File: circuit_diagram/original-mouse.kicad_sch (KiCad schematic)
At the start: 106 parts, among them J1 Conn_02x03_Odd_Even, J2 Conn_02x03_Odd_Even, J3 Conn_01x08, Q1 TJ8S06M3L, Q10 ST-1KL3A, Q2 BSS138, Q3 BSS138, Q4 BSS138, Q5 BSS138, Q6 BSS138, Q7 ST-1KL3A, Q8 ST-1KL3A, Q9 ST-1KL3A, SW1 SW_SPDT, SW2 TS-06104, SW3 TS-06104, SW4 TS-06104, SW5 SW_Push, SW6 SW_Push, U1 NJM7805SDL1, U2 NJM2845DL1-33, U3 PKMCS0909E4000-R1, U4 ICM-20649, U5 DRV8835, U6 STM32F405RGTx

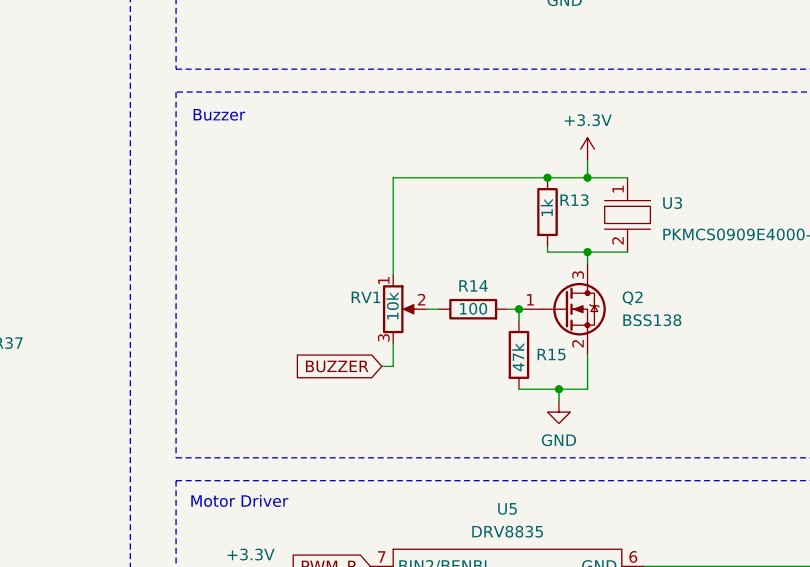
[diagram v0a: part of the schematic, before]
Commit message: ブザー回路を修正
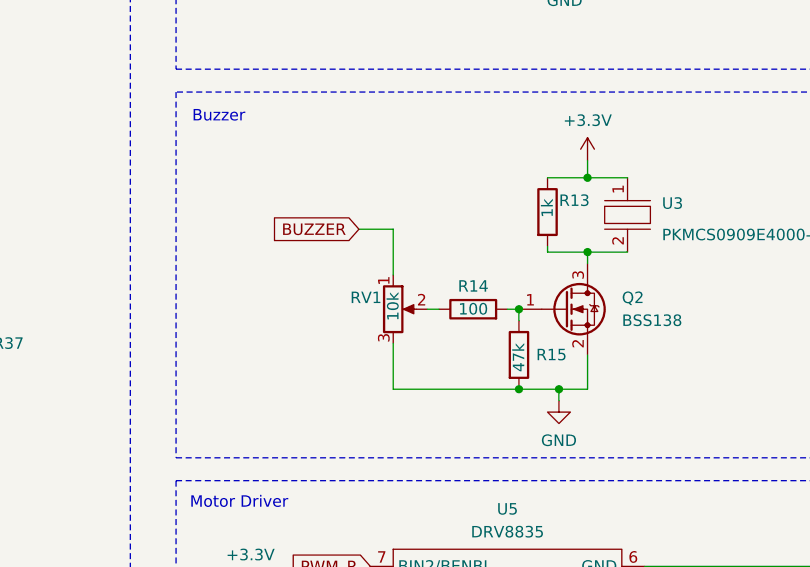
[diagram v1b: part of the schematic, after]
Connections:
- net +3.3V: no longer RV1.1
- net BUZZER: now also RV1.1; no longer RV1.3
- net GND: now also RV1.3
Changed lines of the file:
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@@
   (junction (at 271.78 129.54) (diameter 0) (color 0 0 0 0)
   )
-  (junction (at 353.695 169.545) (diameter 0) (color 0 0 0 0)
-  )
   (junction (at 118.11 264.16) (diameter 0) (color 0 0 0 0)
   )
@@
   )
   (junction (at 237.49 101.6) (diameter 0) (color 0 0 0 0)
+  )
+  (junction (at 350.52 193.04) (diameter 0) (color 0 0 0 0)
   )
   (junction (at 248.92 226.06) (diameter 0) (color 0 0 0 0)
@@
     (stroke (width 0) (type default))
   )
-  (wire (pts (xy 336.55 190.5) (xy 335.28 190.5))
-    (stroke (width 0) (type default))
-  )
   (wire (pts (xy 124.46 194.31) (xy 152.4 194.31))
     (stroke (width 0) (type default))
@@
     (stroke (width 0) (type default))
   )
-  (wire (pts (xy 336.55 169.545) (xy 336.55 180.34))
-    (stroke (width 0) (type default))
-  )
   (wire (pts (xy 89.535 219.075) (xy 89.535 220.98))
     (stroke (width 0) (type default))
@@
     (stroke (width 0) (type default))
   )
+  (wire (pts (xy 336.55 175.26) (xy 332.74 175.26))
+    (stroke (width 0) (type default))
+  )
   (wire (pts (xy 251.46 68.58) (xy 251.46 71.12))
     (stroke (width 0) (type default))
@@
     (stroke (width 0) (type default))
   )
-  (wire (pts (xy 353.695 169.545) (xy 336.55 169.545))
-    (stroke (width 0) (type default))
-  )
   (wire (pts (xy 246.38 119.38) (xy 246.38 127))
     (stroke (width 0) (type default))
@@
     (stroke (width 0) (type default))
   )
+  (wire (pts (xy 336.55 180.34) (xy 336.55 175.26))
+    (stroke (width 0) (type default))
+  )
   (wire (pts (xy 43.18 48.26) (xy 53.34 48.26))
     (stroke (width 0) (type default))
@@
     (stroke (width 0) (type default))
   )
+  (wire (pts (xy 336.55 193.04) (xy 350.52 193.04))
+    (stroke (width 0) (type default))
+  )
   (wire (pts (xy 243.84 116.84) (xy 248.92 116.84))
     (stroke (width 0) (type default))
@@
     (stroke (width 0) (type default))
   )
+  (wire (pts (xy 336.55 187.96) (xy 336.55 193.04))
+    (stroke (width 0) (type default))
+  )
   (wire (pts (xy 108.585 215.9) (xy 108.585 219.075))
     (stroke (width 0) (type default))
@@
   )
   (wire (pts (xy 386.08 223.52) (xy 386.08 225.425))
-    (stroke (width 0) (type default))
-  )
-  (wire (pts (xy 336.55 187.96) (xy 336.55 190.5))
     (stroke (width 0) (type default))
   )
@@
     )
   )
-  (global_label "BUZZER" (shape input) (at 335.28 190.5 180) (fields_autoplaced)
+  (global_label "BUZZER" (shape input) (at 332.74 175.26 180) (fields_autoplaced)
     (effects (font (size 1.27 1.27)) (justify right))
-    (property "Intersheetrefs" "${INTERSHEET_REFS}" (at 324.9357 190.5 0)
+    (property "Intersheetrefs" "${INTERSHEET_REFS}" (at 322.3957 175.26 0)
       (effects (font (size 1.27 1.27)) (justify right) hide)
     )

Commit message: フットプリントの割り当て
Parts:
- BT1: footprint (none) -> Connector_JST:JST_XH_B2B-XH-A_1x02_P2.50mm_Vertical
- C1, C10, C11, C12, C13, C14, C15, C16, C17, C18, C19, C2, C20, C21, C22, C23, C24, C25, C26, C27, C28, C29, C3, C4, C5, C6, C7, C8, C9: footprint (none) -> Capacitor_SMD:C_0603_1608Metric_Pad1.08x0.95mm_HandSolder
- D1: footprint (none) -> Package_TO_SOT_SMD:SOT-23
- D10, D2, D3, D4, D5: footprint (none) -> LED_SMD:LED_0603_1608Metric_Pad1.05x0.95mm_HandSolder
- D6, D7, D8, D9: footprint (none) -> LED_THT:LED_D5.0mm_Horizontal_O3.81mm_Z3.0mm
- FB1: footprint (none) -> RTLIB:IND_BOURNS_1608
- J1, J2: footprint (none) -> Connector_IDC:IDC-Header_2x03_P2.54mm_Vertical
- J3: footprint (none) -> Connector_PinSocket_2.54mm:PinSocket_1x08_P2.54mm_Vertical
- Q1, U1, U2: footprint (none) -> Package_TO_SOT_SMD:TO-252-2
- Q10, Q7, Q8, Q9: footprint (none) -> RTLIB:TR-F
- R1, R10, R11, R12, R13, R14, R15, R16, R17, R18, R19, R2, R20, R21, R22, R23, R24, R25, R26, R27, R28, R29, R3, R30, R31, R32, R33, R34, R35, R36, R37, R38, R39, R4, R5, R6, R7, R8, R9: footprint (none) -> Resistor_SMD:R_0603_1608Metric_Pad0.98x0.95mm_HandSolder
- RV1: footprint (none) -> RTLIB:BOURNS-3362P_pot
- SW1: footprint (none) -> RTLIB:SSSS213202
- SW2, SW3, SW4: footprint (none) -> Button_Switch_SMD:SW_MEC_5GSH9
- SW5, SW6: footprint (none) -> RTLIB:TVAF06-A020B-R
- U3: footprint (none) -> Buzzer_Beeper:Buzzer_Murata_PKMCS0909E
- U4: footprint (none) -> Sensor_Motion:InvenSense_QFN-24_3x3mm_P0.4mm
- U5: footprint (none) -> RTLIB:DRV8835

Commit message: 配線だいたい完了
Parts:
- C6: footprint Capacitor_SMD:C_0603_1608Metric_Pad1.08x0.95mm_HandSolder -> Capacitor_SMD:CP_Elec_6.3x7.7
- SW2, SW3, SW4: value TS-06104 -> SW_Push; footprint Button_Switch_SMD:SW_MEC_5GSH9 -> RTLIB:TVAF06-A020B-R; symbol Switch:SW_MEC_5E -> Switch:SW_Push
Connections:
- net +3.3V: no longer Q10.1 (C), Q7.1 (C), Q8.1 (C), Q9.1 (C)
- net GND: now also SW2.2, SW3.2, SW4.2; no longer SW2.3 (K), SW2.4 (A), SW3.3 (K), SW3.4 (A), SW4.3 (K), SW4.4 (A)
- net LEFT_FRONT_AD: now also C10.2, R33.1; no longer C11.2, R35.1
- net LEFT_SIDE_AD: now also C11.2, R35.1; no longer C9.2, R31.1
- net RIGHT_FRONT_AD: now also C9.2, R31.1; no longer C10.2, R33.1
- net SW0: no longer SW2.2
- net SW1: no longer SW3.2
- net SW2: no longer SW4.2
- net +3.3VA: now reaches C26.1, C27.1, C28.1, FB1.2, U6.13 (VDDA)
- net +3.3VA: now also Q10.1 (C), Q7.1 (C), Q8.1 (C), Q9.1 (C)
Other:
- moved on the sheet: C10, C11, C8, C9, Q10, Q7, Q8, Q9, R28, R29, R30, R31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
